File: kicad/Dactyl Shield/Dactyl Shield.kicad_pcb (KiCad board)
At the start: 4 copper layers, 99.4 x 77.4 mm, 122 parts, among them J201 JST, J202 Split, J203 Column, J204 Thumb, J205 External, J206 Row, J207 Display, J208 Vic, J209 ResA, J212 ResB, J301 JST, J302 Split, J303 Column, J304 Thumb, J305 External, J306 Row, J307 Display, J308 Vic, J309 ResA, J312 ResB, Q201 AO3400A, Q301 AO3400A, SW201 Battery, SW202 Reset, SW203 LED, SW301 Battery, SW302 Reset, SW303 LED, U201 SRV05-4, U202 Nice!Nano/2040, U301 SRV05-4, U302 Nice!Nano/2040

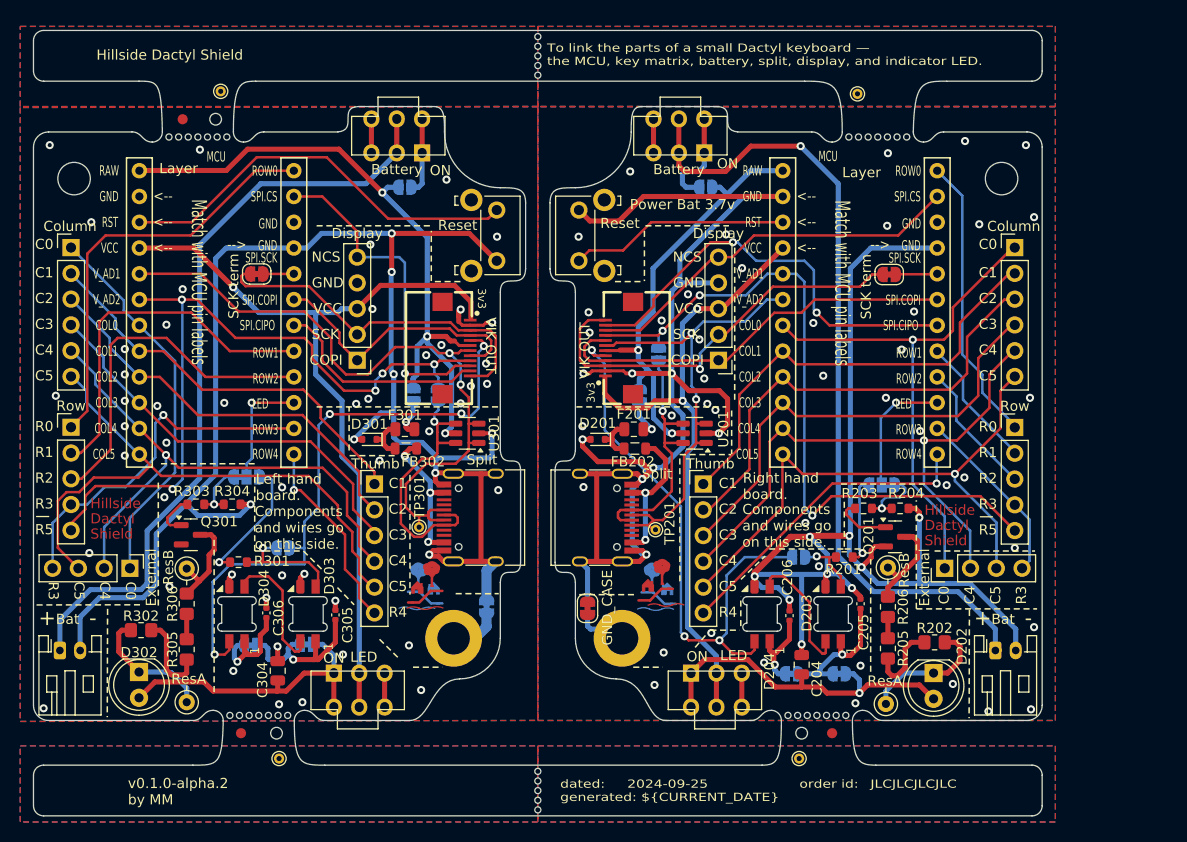
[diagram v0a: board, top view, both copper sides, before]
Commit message: feat: swap power and reset location on right board
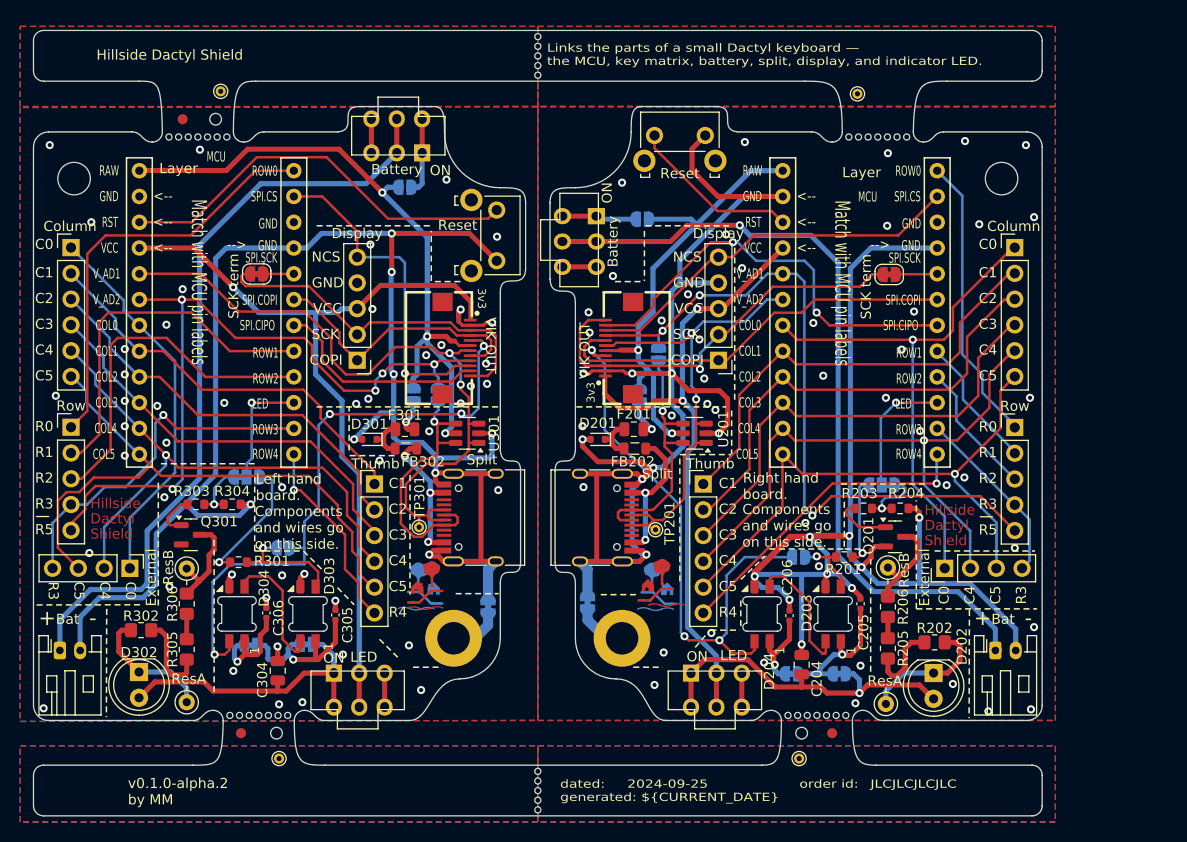
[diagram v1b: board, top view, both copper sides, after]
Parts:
- JP207: moved to B.Cu
- moved SW201 14.3 mm to (143.6, 85.8), turned to -90 degrees
- moved SW202 12.2 mm to (153.5, 76.6), turned to 180 degrees
- moved JP201 7.00 mm to (149.8, 83.6)
- moved JP207 0.55 mm to (144.4, 121.4)
- moved JP307 0.15 mm to (134.6, 121.8)
- moved REF** 0.09 mm to (126.9, 122.0)
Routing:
- net /Right/GND: track 244.3 -> 236.2 mm, vias 60 -> 61
- net /Right/RST: track 21.7 -> 16.9 mm
- net /Right/RAW: track 43.5 -> 46.6 mm
- net /Right/POWER_BAT: track 6.51 -> 4.00 mm
- net /Right/bat+: track 77.1 -> 75.5 mm
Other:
- outline, holes or cut-outs redrawn
- board text added: "Links the parts of a small Dactyl keyboard — the MCU, key matrix, battery, split, display, and indicator LED."
- board text removed: "To link the parts of a small Dactyl keyboard — the MCU, key matrix, battery, split, display, and indicator LED."

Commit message: feat: route ground traces, fix mirror positions
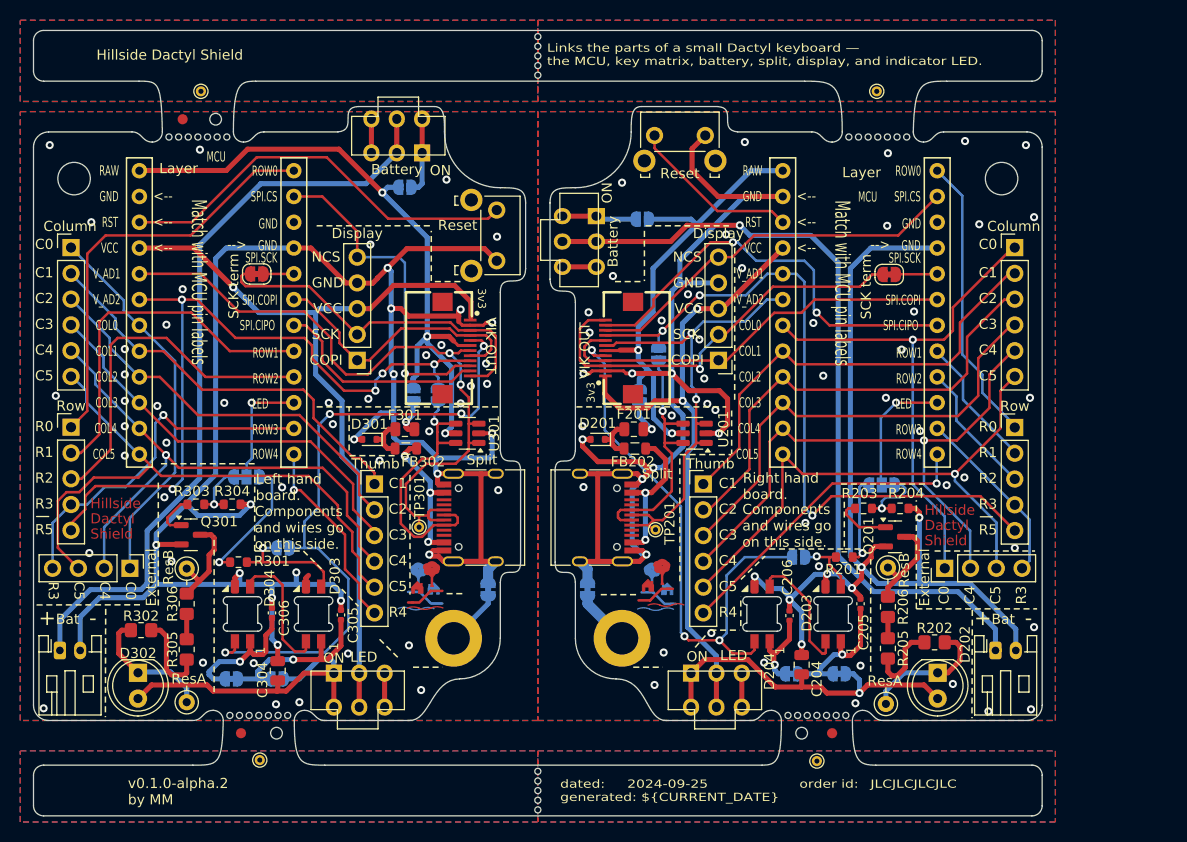
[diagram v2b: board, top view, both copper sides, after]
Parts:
- moved JP309 4.47 mm to (113.8, 128.9)
- moved JP305 3.81 mm to (109.3, 128.9)
- moved TP101 1.95 mm to (106.3, 71.0)
- moved TP102 1.92 mm to (172.9, 71.0)
- moved TP103 1.91 mm to (112.1, 136.9)
- moved TP104 1.77 mm to (167.0, 137.0)
- moved JP307 1.70 mm to (134.6, 120.1)
- moved JP207 1.30 mm to (144.4, 120.1)
- moved D303 0.55 mm to (117.4, 122.5)
- moved D304 0.55 mm to (110.4, 122.5)
- moved C305 0.55 mm to (120.1, 122.6)
- moved C306 0.55 mm to (113.3, 122.4)
- moved D202 0.40 mm to (178.9, 128.3)
- moved D302 0.13 mm to (100.1, 128.3)
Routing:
- net /Left/GND: track 166.2 -> 200.1 mm, vias 56 -> 57
- net /Right/GND: track 236.2 -> 217.2 mm, vias 61 -> 59
- net /Left/LED_out: track 60.1 -> 64.6 mm
- net /Left/VCC_RGB2: track 10.2 -> 13.3 mm
- net /Left/VCC_LED: track 26.3 -> 28.9 mm
- net /Left/VCC_RGB1: track 16.0 -> 17.6 mm
- net Net-(D303-DIN): track 11.7 -> 12.2 mm
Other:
- board text added: "Bare | Smart"
- board text added: "Power"
- board text added: "Smart | Bare"
- board text removed: "RGB Power"

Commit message: feat: update to latest layer detector
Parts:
- moved REF** 4.10 mm to (167.3, 77.6)
- moved REF** 0.22 mm to (104.3, 77.3)
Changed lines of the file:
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@@
 		(fp_arc
 			(start 6.938123 15.132041)
-			(mid 6.337066 14.8831)
+			(mid 6.337062 14.8831)
 			(end 6.088123 14.282041)
 			(stroke
@@
 		(fp_arc
 			(start 8.236041 -15.740877)
-			(mid 8.837089 -15.491924)
+			(mid 8.837086 -15.491923)
 			(end 9.086041 -14.890877)
 			(stroke
@@
 		(fp_arc
 			(start 6.938123 15.132041)
-			(mid 6.337066 14.8831)
+			(mid 6.337062 14.8831)
 			(end 6.088123 14.282041)
 			(stroke
@@
 		(fp_arc
 			(start 8.236041 -15.740877)
-			(mid 8.837089 -15.491924)
+			(mid 8.837086 -15.491923)
 			(end 9.086041 -14.890877)
 			(stroke
@@
 		)
 		(fp_text user "MCU"
-			(at 0 -15.85 0)
+			(at 0 -13.3 0)
 			(layer "F.SilkS")
 			(effects
@@
 	(footprint "Dactyl_basics:art_inner_layer_detector"
 		(layer "F.Cu")
-		(at 104.1 77.2 90)
+		(at 104.3 77.3 90)
 		(property "Reference" "REF**"
 			(at 0 7 90)
@@
 		)
 		(property "Value" "Layer"
-			(at -1.4 0 0)
+			(at 0.05 3.1 0)
 			(unlocked yes)
 			(layer "F.SilkS")
@@
 		)
 		(property "Value2" "Count"
-			(at -1.5 -0.1 180)
+			(at -1.5 -0.1 0)
 			(layer "F.SilkS")
 			(hide yes)
@@
 			(polygon
 				(pts
-					(xy 104.7 78.2) (xy 104.7 76.2) (xy 105.1 76.2) (xy 105.1 78.2)
+					(xy 104.9 78.3) (xy 104.9 76.3) (xy 105.3 76.3) (xy 105.3 78.3)
 				)
 			)
@@
 			(polygon
 				(pts
-					(xy 103.1 78.2) (xy 103.1 76.2) (xy 105.1 76.2) (xy 105.1 78.2)
+					(xy 103.3 78.3) (xy 103.3 76.3) (xy 105.3 76.3) (xy 105.3 78.3)
 				)
 			)
@@
 		)
 	)
-	(footprint "Dactyl_basics:art_inner_layer_detector"
-		(layer "F.Cu")
-		(at 171.4 77.6 90)
-		(property "Reference" "REF**"
-			(at 0 7 90)
-			(unlocked yes)
-			(layer "F.SilkS")
-			(hide yes)
-			(effects
-				(font
-					(size 1 1)
-					(thickness 0.15)
-				)
-			)
-		)
-		(property "Value" "Layer"
-			(at -1.4 0 0)
-			(unlocked yes)
-			(layer "F.SilkS")
-			(effects
-				(font
-					(size 1 1)
-					(thickness 0.15)
-				)
-			)
-		)
-		(property "Footprint" "Dactyl_basics:art_inner_layer_detector"
-			(at 0 7.5 90)
-			(unlocked yes)
-			(layer "F.Fab")
-			(hide yes)
-			(effects
-				(font
-					(size 1 1)
-					(thickness 0.15)
-				)
-			)
-		)
-		(property "Datasheet" ""
-			(at 0 7.5 90)
-			(unlocked yes)
-			(layer "F.Fab")
-			(hide yes)
-			(effects
-				(font
-					(size 1 1)
-					(thickness 0.15)
-				)
-			)
-		)
-		(property "Description" ""
-			(at 0 7.5 90)
-			(unlocked yes)
-			(layer "F.Fab")
-			(hide yes)
-			(effects
-				(font
-					(size 1 1)
-					(thickness 0.15)
-				)
-			)
-		)
-		(property "Value2" "Count"
-			(at -1.5 -0.1 180)
-			(layer "F.SilkS")
-			(hide yes)
-			(effects
-				(font
-					(size 1 1)
-					(thickness 0.15)
-				)
-			)
-		)
-		(solder_mask_margin 2)
-		(clearance 2)
-		(attr smd board_only exclude_from_pos_files exclude_from_bom allow_missing_courtyard
-			dnp
-		)
-		(fp_rect
-			(start -1.1 -1.1)
-			(end 1.1 -0.4)
-			(stroke
-				(width 0.1)
-				(type solid)
-			)
-			(fill solid)
-			(layer "B.Mask")
-		)
-		(fp_rect
-			(start -1.1 0.4)
-			(end 1.1 1.1)
-			(stroke
-				(width 0.1)
-				(type solid)
-			)
-			(fill solid)
-			(layer "B.Mask")
-		)
-		(fp_rect
-			(start -1.1 -1.1)
-			(end 1.1 -0.4)
-			(stroke
-				(width 0.1)
-				(type solid)
-			)
-			(fill solid)
-			(layer "F.Mask")
-		)
-		(fp_rect
-			(start -1.1 0.4)
-			(end 1.1 1.1)
-			(stroke
-				(width 0.1)
-				(type solid)
-			)
-			(fill solid)
-			(layer "F.Mask")
-		)
-		(fp_text user "${REFERENCE}"
-			(at 0 10 90)
-			(unlocked yes)
-			(layer "F.Fab")
-			(effects
-				(font
-					(size 1 1)
-					(thickness 0.15)
-				)
-			)
-		)
-		(zone
-			(net 0)
-			(net_name "")
-			(layers "F.Cu" "In1.Cu" "In2.Cu" "B.Cu")
-			(name "no-outer")
-			(hatch edge 0.5)
-			(connect_pads
-				(clearance 0)
-			)
-			(min_thickness 0.25)
-			(filled_areas_thickness no)
-			(keepout
-				(tracks allowed)
-				(vias allowed)
-				(pads allowed)
-				(copperpour not_allowed)
-				(footprints allowed)
-			)
-			(fill
-				(thermal_gap 0.5)
-				(thermal_bridge_width 0.5)
-			)
-			(polygon
-				(pts
-					(xy 172 78.6) (xy 172 76.6) (xy 172.4 76.6) (xy 172.4 78.6)
-				)
-			)
-		)
-		(zone
-			(net 0)
-			(net_name "")
-			(layers "F&B.Cu")
-			(name "no-outer")
-			(hatch edge 0.5)
-			(connect_pads
-				(clearance 0)
-			)
-			(min_thickness 0.25)
-			(filled_areas_thickness no)
-			(keepout
-				(tracks allowed)
-				(vias allowed)
-				(pads allowed)
-				(copperpour not_allowed)
-				(footprints allowed)
-			)
-			(fill
-				(thermal_gap 0.5)
-				(thermal_bridge_width 0.5)
-			)
-			(polygon
-				(pts
-					(xy 170.4 78.6) (xy 170.4 76.6) (xy 172.4 76.6) (xy 172.4 78.6)
-				)
-			)
-		)
-	)
 	(footprint "Dactyl_basics:SW_Tactile_SKHL_Angled"
 		(layer "F.Cu")
@@
 		)
 	)
+	(footprint "Dactyl_basics:art_inner_layer_detector"
+		(layer "F.Cu")
+		(at 167.3 77.6 90)
+		(property "Reference" "REF**"
+			(at 0 7 90)
+			(unlocked yes)
+			(layer "F.SilkS")
+			(hide yes)
+			(effects
+				(font
+					(size 1 1)
+					(thickness 0.15)
+				)
+			)
+		)
+		(property "Value" "Layer"
+			(at 0.05 3.1 0)
+			(unlocked yes)
+			(layer "F.SilkS")
+			(effects
+				(font
+					(size 1 1)
+					(thickness 0.15)
+				)
+			)
+		)
+		(property "Footprint" "Dactyl_basics:art_inner_layer_detector"
+			(at 0 7.5 90)
+			(unlocked yes)
+			(layer "F.Fab")
+			(hide yes)
+			(effects
+				(font
+					(size 1 1)
+					(thickness 0.15)
+				)
+			)
+		)
+		(property "Datasheet" ""
+			(at 0 7.5 90)
+			(unlocked yes)
+			(layer "F.Fab")
+			(hide yes)
+			(effects
+				(font
+					(size 1 1)
+					(thickness 0.15)
+				)
+			)
+		)
+		(property "Description" ""
+			(at 0 7.5 90)
+			(unlocked yes)
+			(layer "F.Fab")
+			(hide yes)
+			(effects
+				(font
+					(size 1 1)
+					(thickness 0.15)
+				)
+			)
+		)
+		(property "Value2" "Count"
+			(at -1.5 -0.1 0)
+			(layer "F.SilkS")
+			(hide yes)
+			(effects
+				(font
+					(size 1 1)
+					(thickness 0.15)
+				)
+			)
+		)
+		(solder_mask_margin 2)
+		(clearance 2)
+		(attr smd board_only exclude_from_pos_files exclude_from_bom allow_missing_courtyard
+			dnp
+		)
+		(fp_rect
+			(start -1.1 -1.1)
+			(end 1.1 -0.4)
+			(stroke
+				(width 0.1)
+				(type solid)
+			)
+			(fill solid)
+			(layer "B.Mask")
+		)
+		(fp_rect
+			(start -1.1 0.4)
+			(end 1.1 1.1)
+			(stroke
+				(width 0.1)
+				(type solid)
+			)
+			(fill solid)
+			(layer "B.Mask")
+		)
+		(fp_rect
+			(start -1.1 -1.1)
+			(end 1.1 -0.4)
+			(stroke
+				(width 0.1)
+				(type solid)
+			)
+			(fill solid)
+			(layer "F.Mask")
+		)
+		(fp_rect
+			(start -1.1 0.4)
+			(end 1.1 1.1)
+			(stroke
+				(width 0.1)
+				(type solid)
+			)
+			(fill solid)
+			(layer "F.Mask")
+		)
+		(fp_text user "${REFERENCE}"
+			(at 0 10 90)
+			(unlocked yes)
+			(layer "F.Fab")
+			(effects
+				(font
+					(size 1 1)
+					(thickness 0.15)
+				)
+			)
+		)
+		(zone
+			(net 0)
+			(net_name "")
+			(layers "F.Cu" "In1.Cu" "In2.Cu" "B.Cu")
+			(name "no-outer")
+			(hatch edge 0.5)
+			(connect_pads
+				(clearance 0)
+			)
+			(min_thickness 0.25)
+			(filled_areas_thickness no)
+			(keepout
+				(tracks allowed)
+				(vias allowed)
+				(pads allowed)
+				(copperpour not_allowed)
+				(footprints allowed)
+			)
+			(fill
+				(thermal_gap 0.5)
+				(thermal_bridge_width 0.5)
+			)
+			(polygon
+				(pts
+					(xy 167.9 78.6) (xy 167.9 76.6) (xy 168.3 76.6) (xy 168.3 78.6)
+				)
+			)
+		)
+		(zone
+			(net 0)
+			(net_name "")
+			(layers "F&B.Cu")
+			(name "no-outer")
+			(hatch edge 0.5)
+			(connect_pads
+				(clearance 0)
+			)
+			(min_thickness 0.25)
+			(filled_areas_thickness no)
+			(keepout
+				(tracks allowed)
+				(vias allowed)
+				(pads allowed)
+				(copperpour not_allowed)
+				(footprints allowed)
+			)
+			(fill
+				(thermal_gap 0.5)
+				(thermal_bridge_width 0.5)
+			)
+			(polygon
+				(pts
+					(xy 166.3 78.6) (xy 166.3 76.6) (xy 168.3 76.6) (xy 168.3 78.6)
+				)
+			)
+		)
+	)
 	(footprint "Resistor_SMD:R_0805_2012Metric_Pad1.20x1.40mm_HandSolder"
 		(layer "F.Cu")
@@
 	)
 	(via
-		(at 106.2 76.75)
+		(at 106.55 76.4)
 		(size 0.8)
 		(drill 0.4)

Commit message: doc(sck): better notes on split wire use
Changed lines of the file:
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@@
 	(title_block
 		(title "Hillside Dactyl Shield")
-		(date "2024-09-25")
+		(date "2025-01-14")
 		(rev "0.1.0-alpha.2")
+		(comment 4 "Shield for Dactyl split keyboards")
 	)
 	(layers
@@
 		(fp_arc
 			(start 6.938123 15.132041)
-			(mid 6.337062 14.8831)
+			(mid 6.337066 14.8831)
 			(end 6.088123 14.282041)
 			(stroke
@@
 		(fp_arc
 			(start 8.236041 -15.740877)
-			(mid 8.837086 -15.491923)
+			(mid 8.837089 -15.491924)
 			(end 9.086041 -14.890877)
 			(stroke
@@
 		(fp_arc
 			(start 6.938123 15.132041)
-			(mid 6.337062 14.8831)
+			(mid 6.337066 14.8831)
 			(end 6.088123 14.282041)
 			(stroke
@@
 		(fp_arc
 			(start 8.236041 -15.740877)
-			(mid 8.837086 -15.491923)
+			(mid 8.837089 -15.491924)
 			(end 9.086041 -14.890877)
 			(stroke
